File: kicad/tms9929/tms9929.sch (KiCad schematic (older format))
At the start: 47 parts, among them U1 TMS9929A, U2 4164, U3 4164

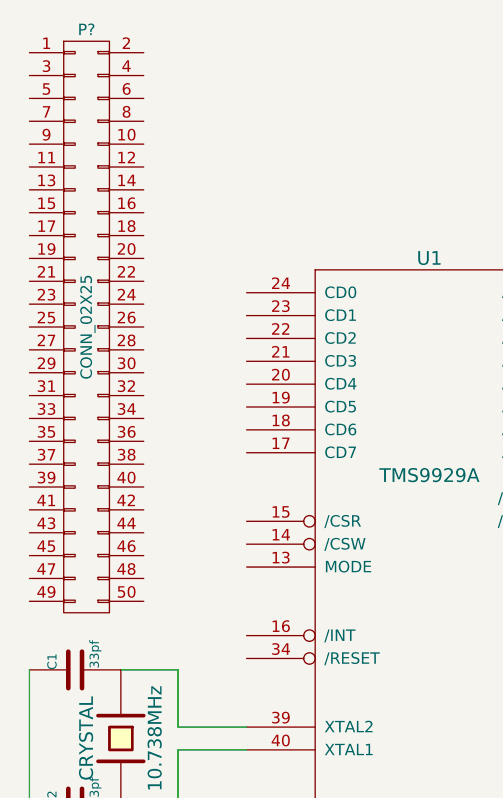
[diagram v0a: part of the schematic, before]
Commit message: +moved vdp to kicad
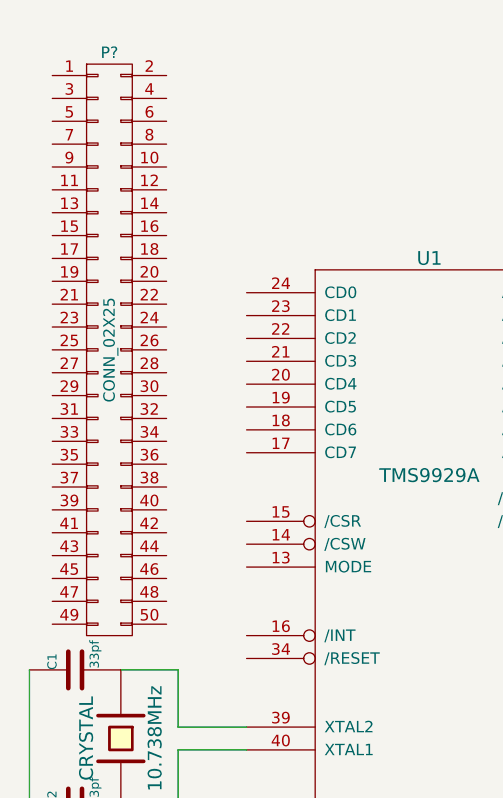
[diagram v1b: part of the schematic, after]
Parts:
- removed P?: CONN_02X25, symbol CONN_02X25
- added P?: CONN_02X25, symbol CONN_02X25
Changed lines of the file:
@@
-$EndComp
-$Comp
-L CONN_02X25 P?
-U 1 1 5419F71F
-P 1050 1800
-F 0 "P?" H 1050 3100 50  0000 C CNN
-F 1 "CONN_02X25" V 1050 1800 50  0000 C CNN
-F 2 "" H 1050 1050 60  0000 C CNN
-F 3 "" H 1050 1050 60  0000 C CNN
-	1    1050 1800
-	1    0    0    -1
 $EndComp
 $Comp
@@
 Wire Wire Line
 	6550 750  6400 750
+$Comp
+L CONN_02X25 P?
+U 1 1 541B3E50
+P 1150 1900
+F 0 "P?" H 1150 3200 50  0000 C CNN
+F 1 "CONN_02X25" V 1150 1900 50  0000 C CNN
+F 2 "" H 1150 1150 60  0000 C CNN
+F 3 "" H 1150 1150 60  0000 C CNN
+	1    1150 1900
+	1    0    0    -1
+$EndComp
 $EndSCHEMATC

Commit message: A1 an DI
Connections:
- net labels added: AD1
- wire segments 140 -> 109
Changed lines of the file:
@@
 	5100 2150 5200 2050
 Wire Bus Line
-	3450 1850 3450 1950
-Wire Bus Line
-	3450 1950 3450 2050
-Wire Bus Line
-	3450 2050 3450 2150
-Wire Bus Line
-	3450 2150 3450 2250
-Wire Bus Line
-	3450 2250 3450 2350
-Wire Bus Line
-	3450 2350 3450 2450
-Wire Bus Line
-	3600 850  3600 950
-Wire Bus Line
-	3600 950  3600 1050
-Wire Bus Line
-	3600 1050 3600 1150
-Wire Bus Line
-	3600 1150 3600 1250
-Wire Bus Line
-	3600 1250 3600 1350
-Wire Bus Line
-	3600 1350 3600 1450
+	3450 1850 3450 2450
+Wire Bus Line
+	3600 850  3600 1450
 Wire Wire Line
 	3700 1450 3700 1500
 Wire Bus Line
-	3450 2650 3450 2750
-Wire Bus Line
-	3450 2750 3450 2850
-Wire Bus Line
-	3600 1950 3600 2050
-Wire Bus Line
-	3600 2050 3600 2150
+	3450 2650 3450 2850
+Wire Bus Line
+	3600 1950 3600 2150
 Wire Wire Line
 	1750 3650 1450 3650
@@
 	1750 4050 1750 4100
 Wire Wire Line
-	800  3300 800  3900
-Wire Wire Line
-	800  3900 800  4100
+	800  3300 800  4100
 Connection ~ 800  3900
 Wire Wire Line
 	12550 1700 12500 1700
 Wire Wire Line
-	12350 1950 12350 2000
-Wire Wire Line
-	12350 2000 12350 2050
+	12350 1950 12350 2050
 Connection ~ 12350 2000
 Wire Wire Line
-	11750 2250 11800 2250
-Wire Wire Line
-	11800 2250 12050 2250
+	11750 2250 12050 2250
 Wire Wire Line
 	12300 2000 12350 2000
@@
 Connection ~ 11800 2250
 Wire Wire Line
-	11250 2250 11300 2250
-Wire Wire Line
-	11300 2250 11350 2250
-Wire Wire Line
-	11300 2250 11300 2450
-Wire Wire Line
-	11300 2450 11300 2700
+	11250 2250 11350 2250
+Wire Wire Line
+	11300 2250 11300 2700
 Connection ~ 11300 2250
 Wire Wire Line
@@
 	11250 2650 12350 2650
 Wire Wire Line
-	12350 2450 12350 2650
-Wire Wire Line
-	12350 2650 12350 2700
+	12350 2450 12350 2700
 Connection ~ 12350 2650
 Wire Wire Line
@@
 	12850 950  12850 1500
 Wire Wire Line
-	9600 950  10450 950
-Wire Wire Line
-	10450 950  12350 950
-Wire Wire Line
-	12350 950  12850 950
-Wire Wire Line
-	12850 950  13250 950
+	9600 950  13250 950
 Wire Wire Line
 	12850 1900 12900 1900
@@
 	11800 3900 11700 3900
 Wire Wire Line
-	11700 3850 11700 3900
-Wire Wire Line
-	11700 3900 11700 3950
+	11700 3850 11700 3950
 Wire Wire Line
 	12850 3350 12850 3400
@@
 	11850 3600 12550 3600
 Wire Wire Line
-	12350 3900 12350 4150
-Wire Wire Line
-	12350 4150 12350 4700
+	12350 3900 12350 4700
 Wire Wire Line
 	11750 4150 12350 4150
 Wire Wire Line
-	11700 4350 11700 4400
-Wire Wire Line
-	11700 4400 11700 4550
-Wire Wire Line
-	11700 4550 11700 4600
+	11700 4350 11700 4600
 Wire Wire Line
 	11650 4550 11700 4550
@@
 Connection ~ 11700 3350
 Wire Wire Line
-	10350 4550 10600 4550
-Wire Wire Line
-	10600 4550 11150 4550
-Wire Wire Line
-	10350 4400 10350 4550
-Wire Wire Line
-	10350 4550 10350 4600
+	10350 4550 11150 4550
+Wire Wire Line
+	10350 4400 10350 4600
 Connection ~ 10350 4550
 Wire Wire Line
 	9950 4600 9950 4200
 Wire Wire Line
-	9500 4200 9950 4200
-Wire Wire Line
-	9950 4200 10050 4200
+	9500 4200 10050 4200
 Wire Wire Line
 	12350 5100 12350 5150
@@
 	11800 5800 11700 5800
 Wire Wire Line
-	11700 5750 11700 5800
-Wire Wire Line
-	11700 5800 11700 5850
+	11700 5750 11700 5850
 Wire Wire Line
 	12850 5250 12850 5300
@@
 	11850 5500 12550 5500
 Wire Wire Line
-	12350 5800 12350 6050
-Wire Wire Line
-	12350 6050 12350 6600
+	12350 5800 12350 6600
 Wire Wire Line
 	11750 6050 12350 6050
 Wire Wire Line
-	11700 6250 11700 6300
-Wire Wire Line
-	11700 6300 11700 6450
-Wire Wire Line
-	11700 6450 11700 6500
+	11700 6250 11700 6500
 Wire Wire Line
 	11650 6450 11700 6450
@@
 Connection ~ 11700 5250
 Wire Wire Line
-	10350 6450 10500 6450
-Wire Wire Line
-	10500 6450 11150 6450
-Wire Wire Line
-	10350 6300 10350 6450
-Wire Wire Line
-	10350 6450 10350 6500
+	10350 6450 11150 6450
+Wire Wire Line
+	10350 6300 10350 6500
 Connection ~ 10350 6450
 Wire Wire Line
 	9950 6500 9950 6100
 Wire Wire Line
-	9500 6100 9950 6100
-Wire Wire Line
-	9950 6100 10050 6100
+	9500 6100 10050 6100
 Wire Wire Line
 	12350 7000 12350 7050
@@
 	12850 5700 12850 5750
 Wire Wire Line
-	9600 5250 11700 5250
-Wire Wire Line
-	11700 5250 12850 5250
-Wire Wire Line
-	9600 950  9600 3350
-Wire Wire Line
-	9600 3350 9600 5250
-Wire Wire Line
-	9600 5250 9600 6550
+	9600 5250 12850 5250
+Wire Wire Line
+	9600 950  9600 6550
 Connection ~ 9600 3350
 Connection ~ 9600 5250
@@
 	10350 950  10350 2100
 Wire Wire Line
-	10350 2500 10350 2650
-Wire Wire Line
-	10350 2650 10350 2700
-Wire Wire Line
-	9950 1250 9950 2300
-Wire Wire Line
-	9950 2300 9950 2700
-Wire Wire Line
-	9300 2300 9950 2300
-Wire Wire Line
-	9950 2300 10050 2300
+	10350 2500 10350 2700
+Wire Wire Line
+	9950 1250 9950 2700
+Wire Wire Line
+	9300 2300 10050 2300
 Wire Wire Line
 	10350 3200 10350 3250
@@
 	12350 3200 12350 3250
 Wire Wire Line
-	10350 2650 10700 2650
-Wire Wire Line
-	10700 2650 10750 2650
+	10350 2650 10750 2650
 Connection ~ 10350 2650
 Connection ~ 10450 950
@@
 	11150 4400 10700 4400
 Wire Wire Line
-	10700 2650 10700 4400
-Wire Wire Line
-	10700 4400 10700 6300
+	10700 2650 10700 6300
 Connection ~ 10700 2650
 Wire Wire Line
@@
 	10350 5900 10350 5250
 Wire Wire Line
-	9600 3350 11700 3350
-Wire Wire Line
-	11700 3350 12850 3350
+	9600 3350 12850 3350
 Wire Wire Line
 	10750 2250 10500 2250
@@
 Connection ~ 9950 6100
 Wire Bus Line
-	5100 850  5100 950
-Wire Bus Line
-	5100 950  5100 1050
-Wire Bus Line
-	5100 1050 5100 1150
-Wire Bus Line
-	5100 1150 5100 1250
-Wire Bus Line
-	5100 1250 5100 1350
-Wire Bus Line
-	5100 1350 5100 1450
+	5100 600  5100 1450
 Wire Wire Line
 	5200 1450 5200 1500
 Wire Bus Line
-	5100 1950 5100 2050
-Wire Bus Line
-	5100 2050 5100 2150
+	5100 1950 5100 2150
 Wire Wire Line
 	3350 3650 3500 3650
@@
 	3600 3550 3600 2250
 Wire Wire Line
-	6550 2250 3600 2250
-Wire Wire Line
-	6550 750  6550 2250
+	3600 2250 6550 2250
+Wire Wire Line
+	6550 2250 6550 750
 Wire Wire Line
 	6550 750  6400 750
@@
 	1    0    0    -1
 $EndComp
+Wire Bus Line
+	5100 600  6700 600
+Wire Bus Line
+	6700 600  6700 1050
+Entry Wire Line
+	6600 950  6700 850
+Wire Wire Line
+	6400 950  6600 950
+Text Label 6550 950  0    60   ~ 0
+AD1
+Text Label 3300 1750 0    60   ~ 0
+AD1
 $EndSCHEMATC

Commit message: +update sch
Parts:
- removed P?: CONN_02X25, symbol CONN_02X25
- added C3: 30pF, symbol CTRIM
- added C? (x9): 100nF, symbol C
- added U4, U5, U? (x4): 4164, symbol 4164
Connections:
- net labels added: AD0, AD2, AD3, AD4, AD5, AD6, AD7, CAS, RAS, VAD, VCC, WE
- wire segments 109 -> 169
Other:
- moved on the sheet: C1, C2, C?, Q?, R?, RV?

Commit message: +update
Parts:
- gave numbers to parts that had none: 53
- renumbered 10.738MHz to 10.738MHz1
